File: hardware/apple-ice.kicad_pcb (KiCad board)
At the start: 2 copper layers, 100 x 77.7 mm, 82 parts, among them J1 TO_SP_DRIVE, J2 USB_B_Micro, J3 SPI_FLASH_PROG, P1 A2Bus-apple2, SW1 SW_Push, SW2 SW_Push, SW3 SW_Push, U1 SN74LVC8T245PW, U10 W25Q16JVSS, U2 SN74LVC8T245PW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

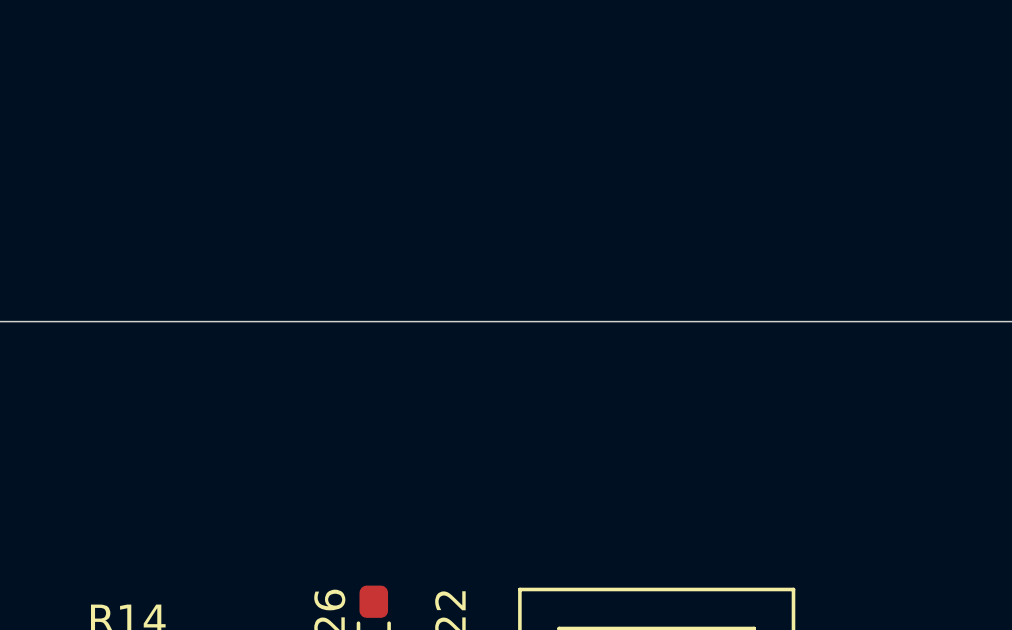
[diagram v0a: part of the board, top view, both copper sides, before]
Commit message: Add 2x15 pin header
Signed-off-by: Rangel Ivanov <rangelivanov88@gmail.com>
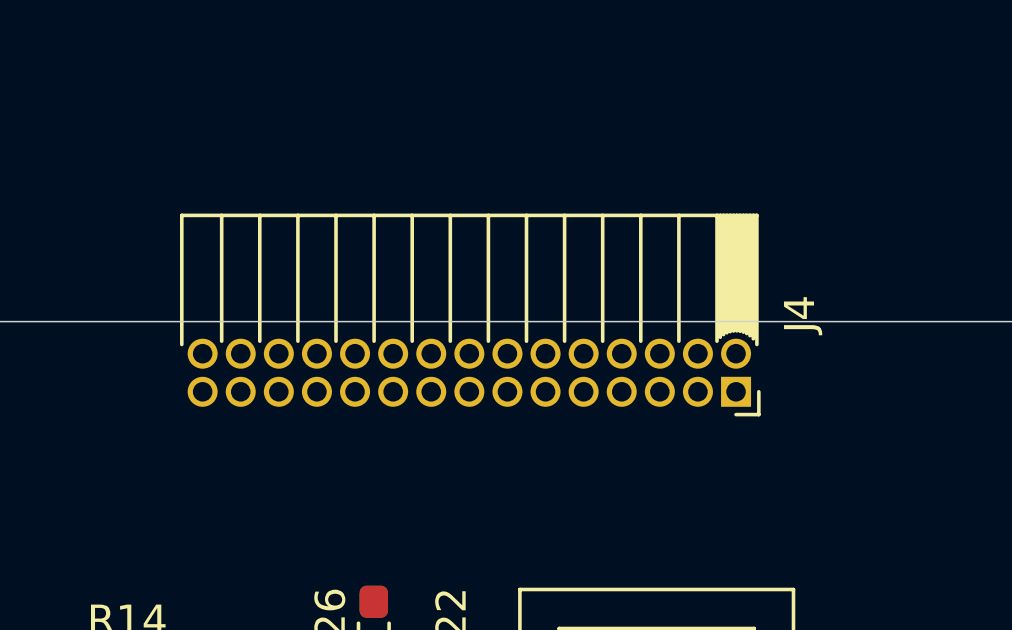
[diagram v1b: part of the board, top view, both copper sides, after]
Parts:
- added J4: Conn_02x15_Odd_Even, apple-ice:PinSocket_2x15_P1.27mm_Horizontal, F.Cu at (179.9, 47.4)

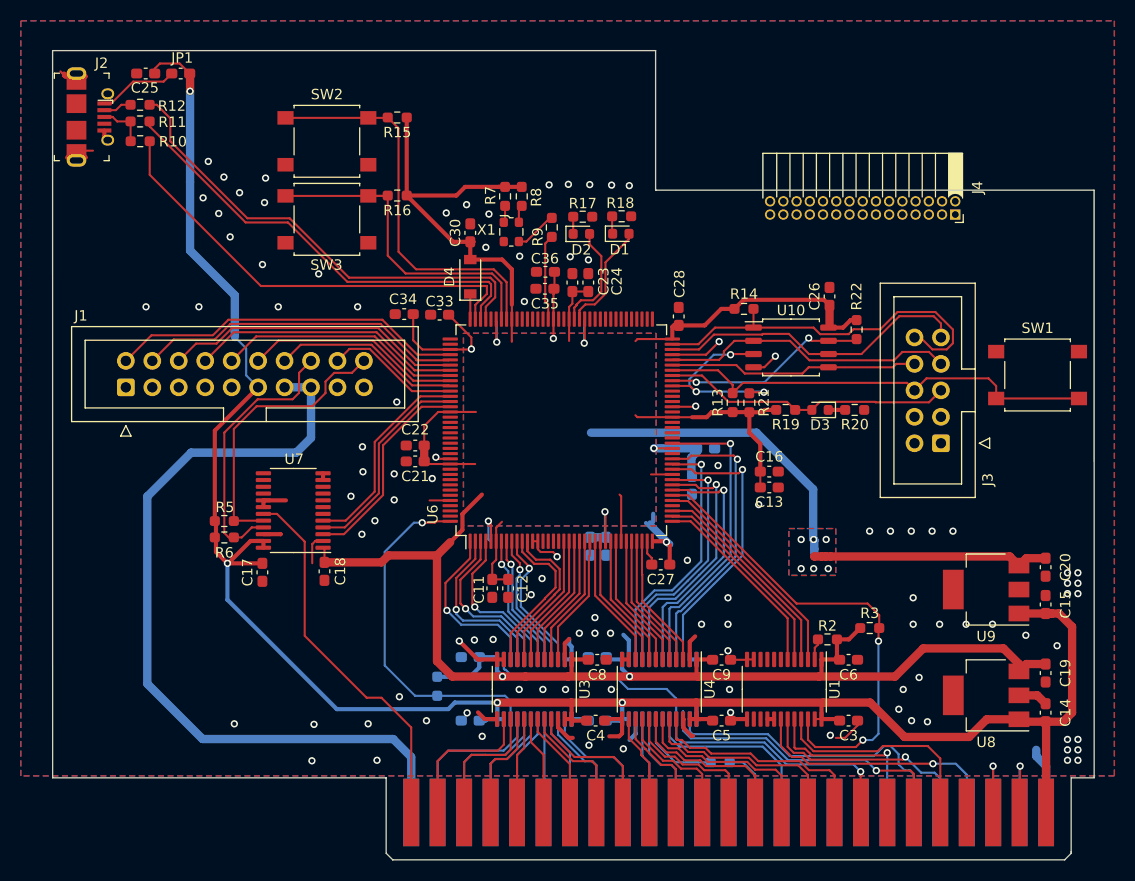
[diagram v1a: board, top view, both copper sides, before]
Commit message: Route double pmod header
Signed-off-by: Rangel Ivanov <rangelivanov88@gmail.com>
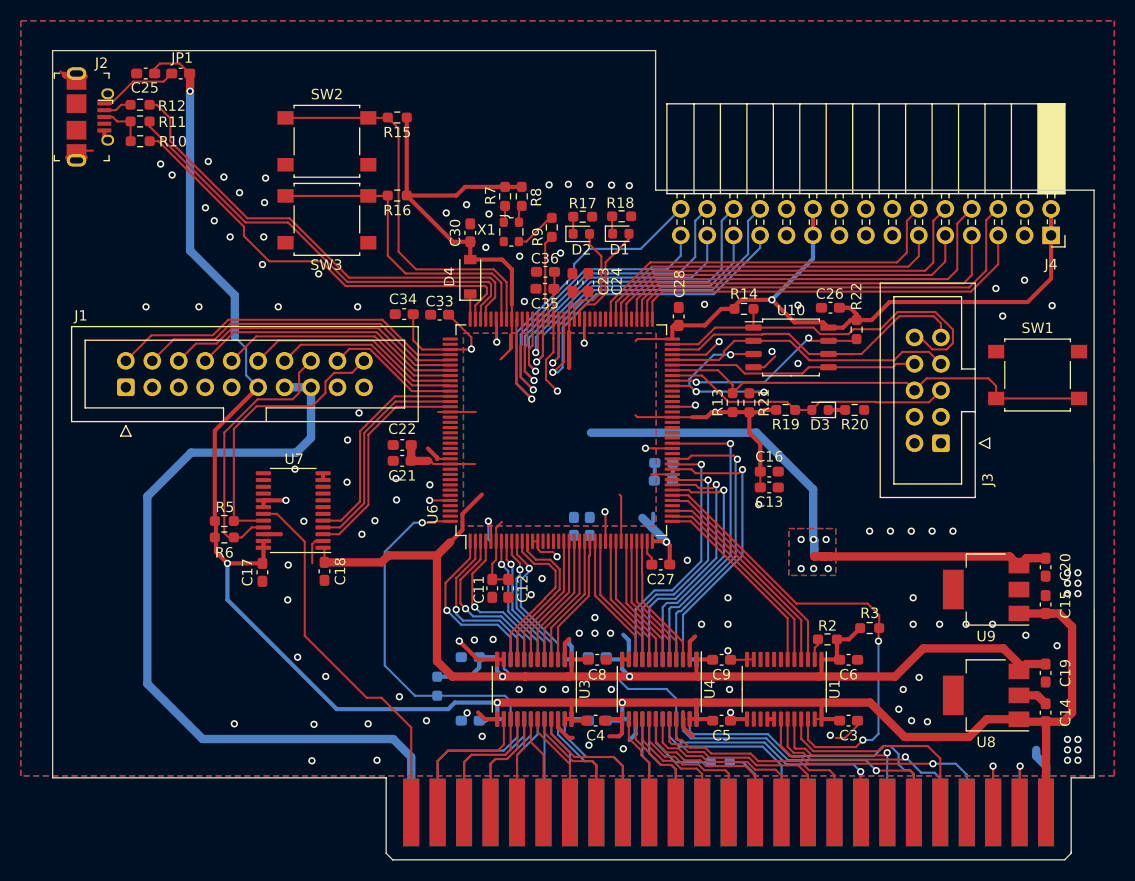
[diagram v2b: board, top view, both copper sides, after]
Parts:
- J4: footprint apple-ice:PinSocket_2x15_P1.27mm_Horizontal -> apple-ice:PinSocket_2x15_P2.54mm_Horizontal
- moved J4 9.41 mm to (189.1, 49.4)
- moved C37 4.25 mm to (151.9, 71.3)
- moved C32 2.80 mm to (151.9, 73.0), turned to 0 degrees
- moved C29 2.45 mm to (143.3, 77.4)
- moved C31 2.45 mm to (144.8, 77.4)
- moved C21 1.25 mm to (126.8, 71.1)
- moved C22 1.25 mm to (126.8, 69.5)
- moved C26 1.09 mm to (167.9, 56.4), turned to 180 degrees
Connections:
- J4 pad 1: Net-(J4-Pad1) -> +3.3V
- J4 pad 10: Net-(J4-Pad10) -> /PMOD_5
- J4 pad 11: Net-(J4-Pad11) -> /PMOD_6
- J4 pad 12: Net-(J4-Pad12) -> /PMOD_7
- J4 pad 19: Net-(J4-Pad19) -> +3.3V
- J4 pad 2: Net-(J4-Pad2) -> +3.3V
- J4 pad 20: Net-(J4-Pad20) -> +3.3V
- J4 pad 21: Net-(J4-Pad21) -> GND
- J4 pad 22: Net-(J4-Pad22) -> GND
- J4 pad 23: Net-(J4-Pad23) -> /PMOD1_0
- J4 pad 24: Net-(J4-Pad24) -> /PMOD1_1
- J4 pad 25: Net-(J4-Pad25) -> /PMOD1_2
- J4 pad 26: Net-(J4-Pad26) -> /PMOD1_3
- J4 pad 27: Net-(J4-Pad27) -> /PMOD1_4
- J4 pad 28: Net-(J4-Pad28) -> /PMOD1_5
- J4 pad 29: Net-(J4-Pad29) -> /PMOD1_6
- J4 pad 3: Net-(J4-Pad3) -> GND
- J4 pad 30: Net-(J4-Pad30) -> /PMOD1_7
- J4 pad 4: Net-(J4-Pad4) -> GND
- J4 pad 5: Net-(J4-Pad5) -> /PMOD_0
- J4 pad 6: Net-(J4-Pad6) -> /PMOD_1
- J4 pad 7: Net-(J4-Pad7) -> /PMOD_2
- J4 pad 8: Net-(J4-Pad8) -> /PMOD_3
- J4 pad 9: Net-(J4-Pad9) -> /PMOD_4
- U6 pad 73: Net-(U6-Pad73) -> /PMOD_0
- U6 pad 74: Net-(U6-Pad74) -> /PMOD_1
- U6 pad 75: Net-(U6-Pad75) -> /PMOD_2
- U6 pad 76: Net-(U6-Pad76) -> /PMOD_3
- U6 pad 78: Net-(U6-Pad78) -> /PMOD_4
- U6 pad 79: Net-(U6-Pad79) -> /PMOD_5
- U6 pad 80: Net-(U6-Pad80) -> /PMOD_6
- U6 pad 81: Net-(U6-Pad81) -> /PMOD_7
- U6 pad 90: Net-(U6-Pad90) -> /PMOD1_0
- U6 pad 91: Net-(U6-Pad91) -> /PMOD1_1
- U6 pad 94: Net-(U6-Pad94) -> /PMOD1_2
- U6 pad 95: Net-(U6-Pad95) -> /PMOD1_3
- U6 pad 96: Net-(U6-Pad96) -> /PMOD1_4
- U6 pad 97: Net-(U6-Pad97) -> /PMOD1_5
- U6 pad 98: Net-(U6-Pad98) -> /PMOD1_6
- U6 pad 99: Net-(U6-Pad99) -> /PMOD1_7
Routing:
- net +3.3V: track 243.2 -> 289.9 mm, vias 2 -> 3
- net /PMOD_1: track 0.00 -> 42.0 mm
- net /PMOD_3: track 0.00 -> 40.3 mm
- net /PMOD_0: track 0.00 -> 39.2 mm
- net /PMOD_5: track 0.00 -> 38.8 mm
- net /PMOD_2: track 0.00 -> 38.3 mm
- net /PMOD_7: track 0.00 -> 36.7 mm
- net /PMOD1_7: track 0.00 -> 36.6 mm, vias 0 -> 1
- net /PMOD_4: track 0.00 -> 36.3 mm
- net /PMOD1_5: track 0.00 -> 35.6 mm, vias 0 -> 1
- net /PMOD_6: track 0.00 -> 34.5 mm
- net /PMOD1_1: track 0.00 -> 34.1 mm, vias 0 -> 1
- net /PMOD1_0: track 0.00 -> 33.9 mm, vias 0 -> 1
- net /PMOD1_6: track 0.00 -> 33.6 mm, vias 0 -> 1
- net /PMOD1_3: track 0.00 -> 31.6 mm, vias 0 -> 1
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
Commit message: Add 5, 12 and -12 power rails to pmod connection
Signed-off-by: Rangel Ivanov <rangelivanov88@gmail.com>
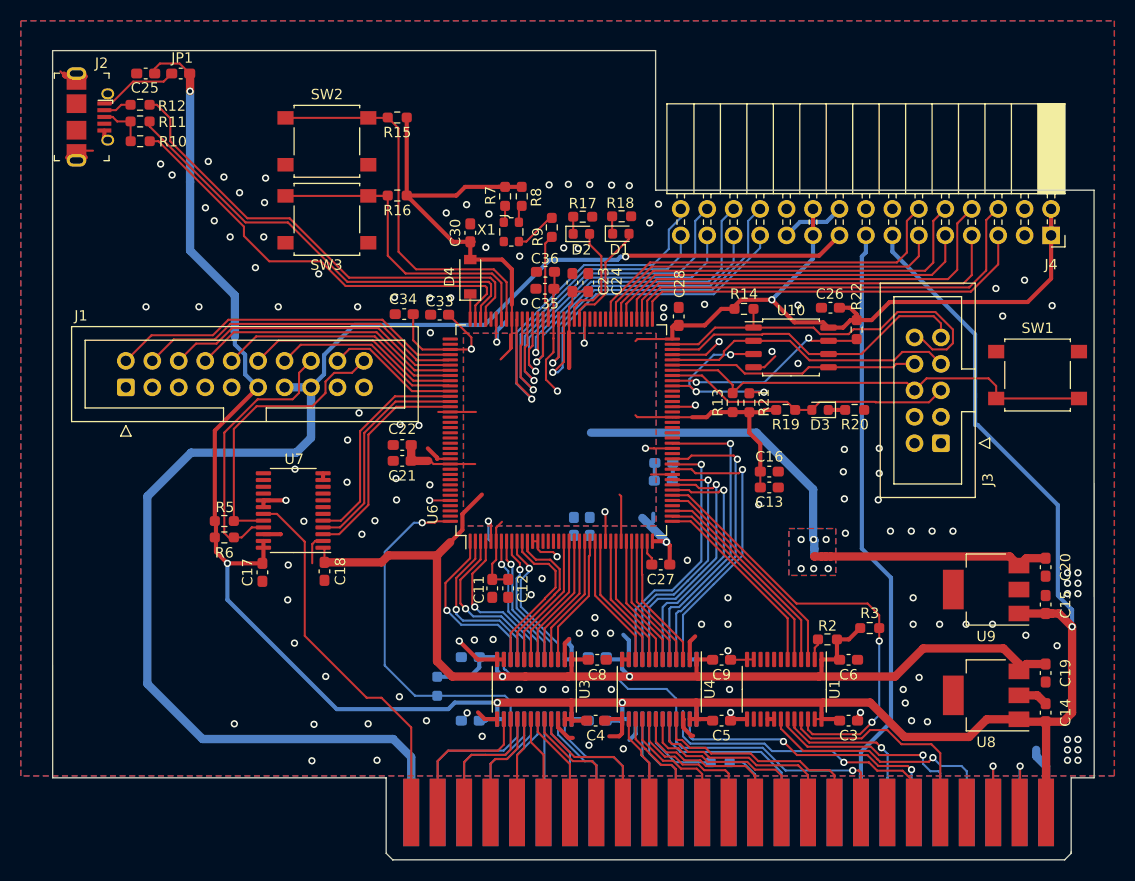
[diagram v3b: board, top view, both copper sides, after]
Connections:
- J4 pad 13: Net-(J4-Pad13) -> +5V
- J4 pad 14: Net-(J4-Pad14) -> GND
- J4 pad 15: Net-(J4-Pad15) -> -12V
- J4 pad 16: Net-(J4-Pad16) -> GND
- J4 pad 17: Net-(J4-Pad17) -> +12V
- J4 pad 18: Net-(J4-Pad18) -> GND
- P1 pad 33: Net-(P1-Pad33) -> -12V
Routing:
- net -12V: track 0.00 -> 57.9 mm
- net +12V: track 77.0 -> 134.9 mm, vias 0 -> 1
- net +5V: track 196.9 -> 242.2 mm, vias 4 -> 5
- net GND: track 99.4 -> 103.6 mm, vias 121 -> 138
- net Net-(R3-Pad2): track 45.6 -> 43.0 mm
- net Net-(P1-Pad32): track 17.8 -> 19.8 mm
- net /PMOD1_7: track 36.6 -> 37.6 mm
- net /~RES: track 29.4 -> 28.5 mm, vias 0 -> 2
- net Net-(P1-Pad30): track 22.1 -> 21.5 mm

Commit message: Add some useful text to the PCB
Signed-off-by: Rangel Ivanov <rangelivanov88@gmail.com>
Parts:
- moved C3 0.44 mm to (169.4, 96.4)
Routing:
- net +5V: track 242.2 -> 243.5 mm
- net Net-(P1-Pad21): track 24.7 -> 24.0 mm
- net /~RES: track 28.5 -> 29.1 mm
- net GND: track 103.6 -> 103.2 mm, vias 138 -> 137
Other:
- board text added: "Apple iCE rev 0.1"
- board text added: "PMOD Expansion"
- board text added: "Smart Port Device"
- board text added: "USB programming and serial comms"
- board text added: "iCE Prog"
- board text added: "iCE reset"
